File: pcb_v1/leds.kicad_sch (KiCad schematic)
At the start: 130 parts

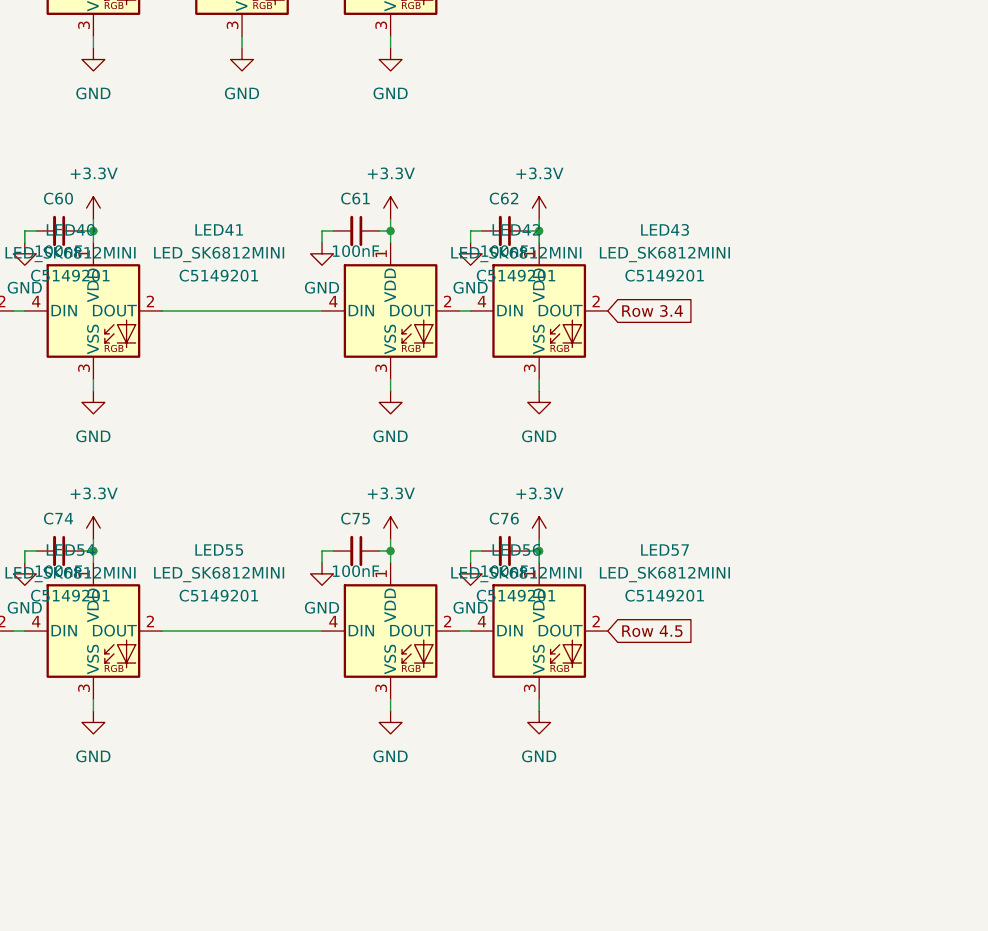
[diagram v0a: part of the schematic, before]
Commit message: Changed PCB to Accommodate Revised Layout
Added a few more keys to balance the screen being 2u x 2u, therefore extending the length of the PCB
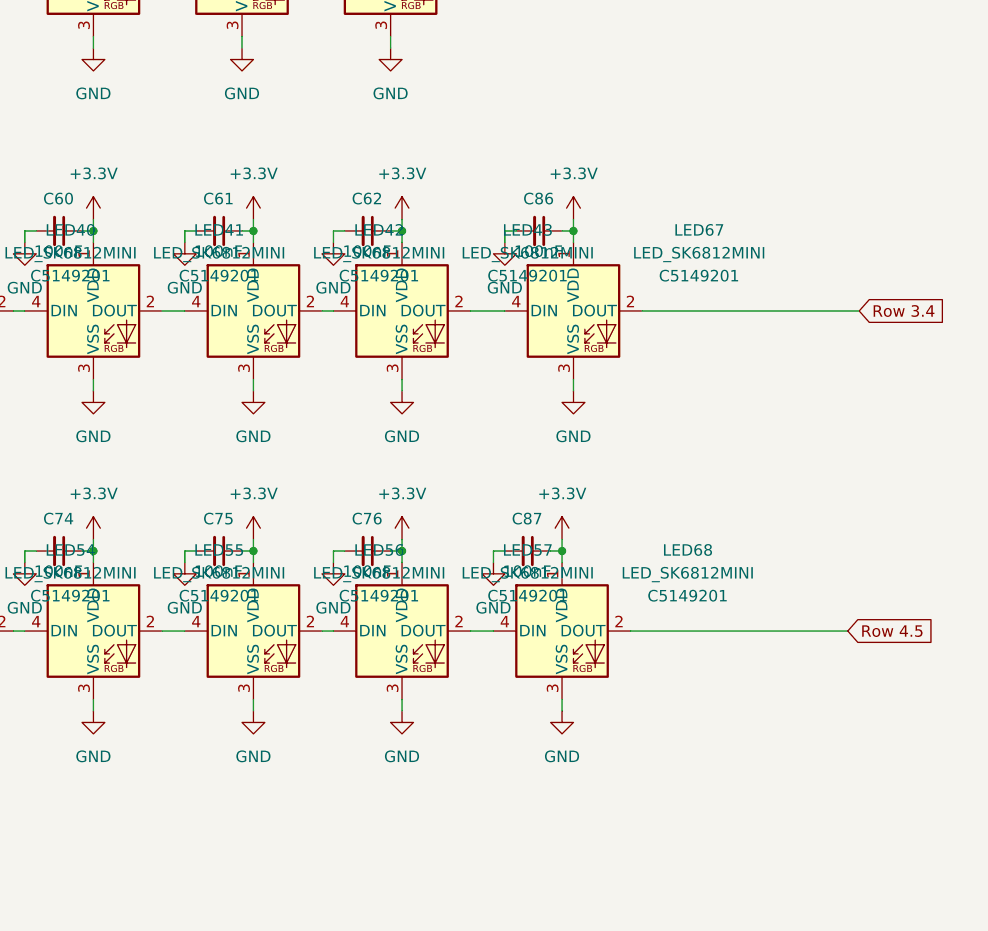
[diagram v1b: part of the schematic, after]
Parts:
- added C86, C87: 100nF, Murata Capacitor:CAPC1608X90N, symbol Device:C_Small
- added LED67, LED68: LED_SK6812MINI, ScottoKeebs_Components:LED_SK6812MINI, symbol ScottoKeebs:LED_SK6812MINI
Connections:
- net +3.3V: now also C86.1, C87.1, LED67.1 (VDD), LED68.1 (VDD)
- net GND: now also C86.2, C87.2, LED67.3 (VSS), LED68.3 (VSS)
- net Row 3.4: now also LED67.2 (DOUT); no longer LED43.2 (DOUT)
- net Row 4.5: now also LED68.2 (DOUT); no longer LED57.2 (DOUT)
- new net: LED43.2 (DOUT), LED67.4 (DIN)
- new net: LED57.2 (DOUT), LED68.4 (DIN)
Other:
- moved on the sheet: C61, C62, C75, C76, LED42, LED43, LED56, LED57
